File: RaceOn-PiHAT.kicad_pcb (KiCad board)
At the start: 2 copper layers, 65 x 56.5 mm, 75 parts, among them IC1 MIC29302WU, IC10 SN74LVC2G07, IC2 NCP5901B, IC3 NCP5901B, IC4 BD48K60G, IC5 LMR14030, IC6 MPU-9250, IC7 SN74LVC2G07, IC8 SN74LVC2G07, IC9 SN74LVC2G07, J1 Screw_Terminal_01x02, J2 Conn_02x03_Odd_Even, J3 Pi Connector, J4 Screw_Terminal_01x02, M1 SERVO, Q1 IPD50R380CE, Q2 IPD50R380CE, Q3 SQJA37EP1, Q4 IPD50R380CE, Q5 IPD50R380CE, U1 CAT24C256, U5 SPX3819M5-L-1-8

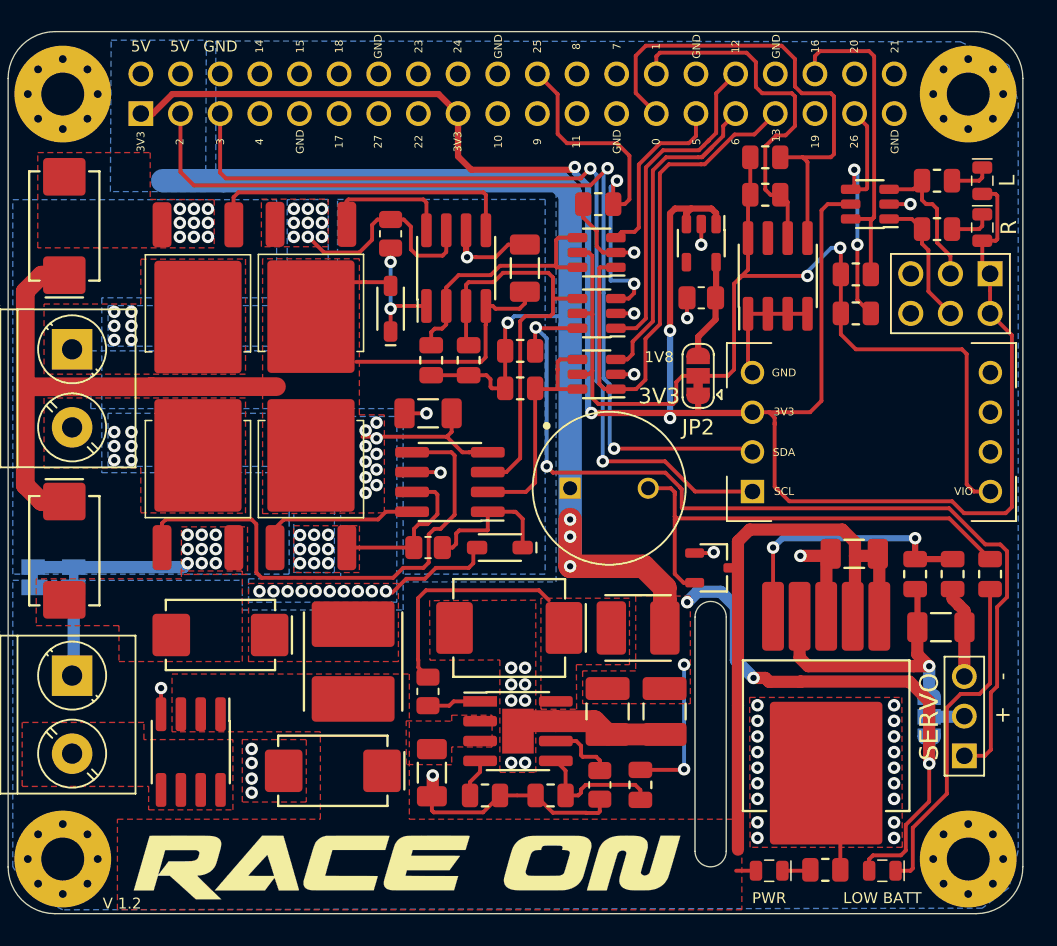
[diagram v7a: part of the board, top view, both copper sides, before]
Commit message: Reposition IMU and fix labels
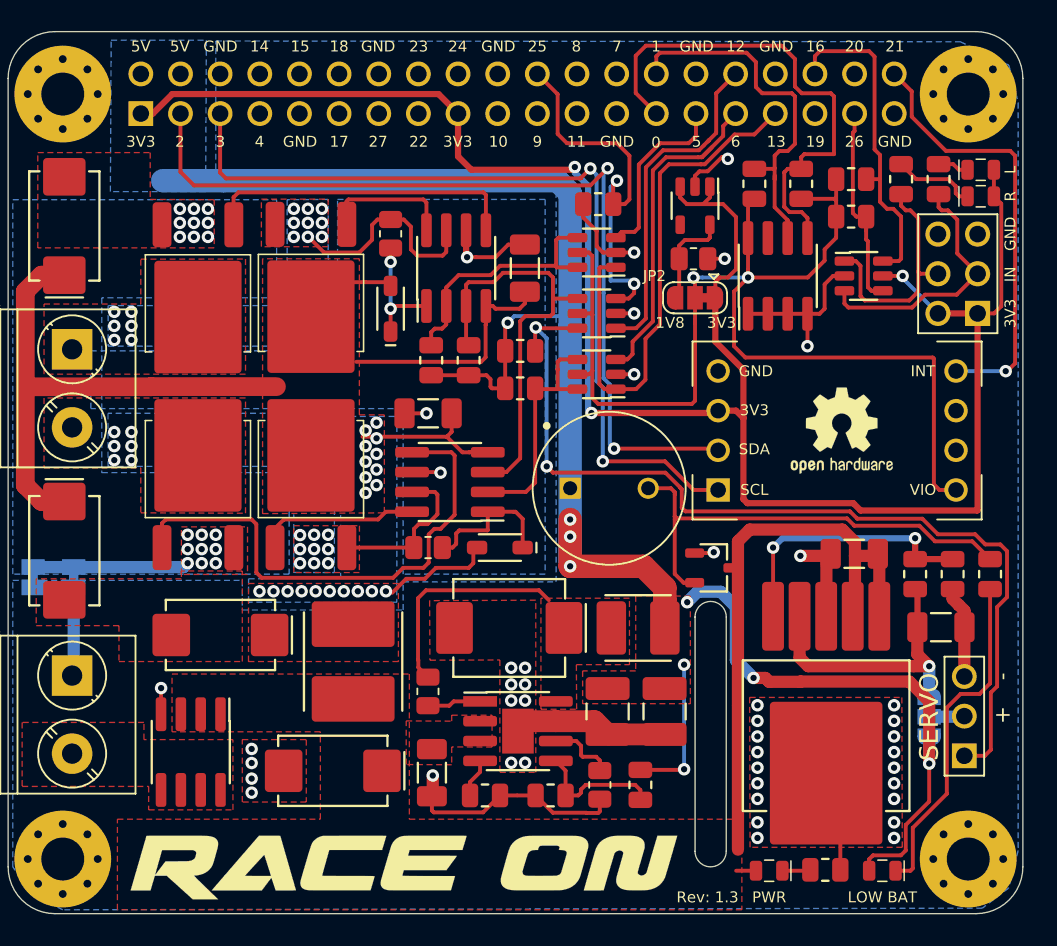
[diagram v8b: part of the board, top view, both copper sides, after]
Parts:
- added LOGO2: Logo_Open_Hardware_Small, Symbol:OSHW-Logo2_7.3x6mm_SilkScreen, F.Cu at (170.4, 87.3)
- moved R17 6.21 mm to (171.0, 73.6)
- moved R16 6.11 mm to (171.0, 71.2)
- moved JP2 5.00 mm to (161.0, 78.8), turned to 180 degrees
- moved IC10 4.62 mm to (171.8, 77.4), turned to 270 degrees
- moved R19 3.94 mm to (174.2, 71.2), turned to 90 degrees
- moved R12 2.86 mm to (167.8, 71.5), turned to 270 degrees
- moved J2 2.66 mm to (179.1, 79.8), turned to 90 degrees
- moved C9 2.55 mm to (160.9, 76.3), turned to 180 degrees
- moved U5 2.43 mm to (161.0, 72.9)
- moved IC6 2.20 mm to (170.1, 87.3)
- moved LED4 2.00 mm to (179.3, 72.3), turned to 0 degrees
- moved R13 0.99 mm to (164.8, 71.5), turned to 270 degrees
- moved LED3 0.71 mm to (179.3, 70.6), turned to 0 degrees
- moved LOGO1 0.20 mm to (142.5, 115.2)
- moved R18 0.14 mm to (176.6, 71.2), turned to 90 degrees
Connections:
- IC6 pad 5: Net-(IC6-Pad5) -> BCM21
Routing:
- net BCM21: track 0.00 -> 28.2 mm, vias 0 -> 1
- net +3V3: track 140.7 -> 129.7 mm, vias 4 -> 3
- net VDD: track 68.7 -> 77.0 mm
- net ENC_L: track 9.29 -> 16.7 mm
- net ENC_R: track 8.53 -> 15.3 mm
- net BCM26: track 17.2 -> 13.8 mm, vias 2 -> 0
- net GND: track 69.4 -> 72.4 mm
- net Net-(LED4-Pad1): track 2.77 -> 5.36 mm
- net BCM3: track 57.4 -> 55.2 mm
- net BCM2: track 59.2 -> 57.0 mm
- net Net-(LED3-Pad1): track 2.67 -> 2.00 mm
- net BCM1: track 23.4 -> 24.0 mm
- net BCM0: track 32.1 -> 32.7 mm
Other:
- board text added: "IN"
- board text added: "INT"
- board text added: "LOW BAT"
- board text added: "Rev: 1.3"
- board text removed: "LOW BATT"
- board text removed: "V 1.2"
